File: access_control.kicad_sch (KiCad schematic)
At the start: 64 parts, among them J1 Conn_01x04_Pin, J10 Screw_Terminal_01x02, J2 Screw_Terminal_01x04, J3 Screw_Terminal_01x04, J4 Screw_Terminal_01x02, J5 Screw_Terminal_01x04, J6 Screw_Terminal_01x04, J7 Screw_Terminal_01x02, J8 Screw_Terminal_01x02, J9 Screw_Terminal_01x02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

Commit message: ERC check verified
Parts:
- U3, U4: Manufacturer Part Number MAX3232ESE+ -> (none)
- U5: footprint Package_TO_SOT_THT:TO-220-3_Vertical -> (none)
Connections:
- net C1+ renamed U3_C1+
- net U3_C1+: no longer C20.1, U4.1 (C1+)
- net C1- renamed U3_C1-
- net U3_C1-: no longer C20.2, U4.3 (C1-)
- net C2+ renamed U3_C2+
- net U3_C2+: no longer C21.1, U4.4 (C2+)
- net C2- renamed U3_C2-
- net U3_C2-: no longer C21.2, U4.5 (C2-)
- net V+ renamed U3_V+
- net U3_V+: no longer C23.1, U4.2 (V+)
- net V- renamed U3_V-
- net U3_V-: no longer C24.1, U4.6 (V-)
- new net U4_C1+: C20.1, U4.1 (C1+)
- new net U4_C1-: C20.2, U4.3 (C1-)
- new net U4_C2+: C21.1, U4.4 (C2+)
- new net U4_C2-: C21.2, U4.5 (C2-)
- new net U4_V+: C23.1, U4.2 (V+)
- new net U4_V-: C24.1, U4.6 (V-)
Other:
- moved on the sheet: C1, C2, C20, C21, C22, C23, C24, C3, C4, C5, D1, D2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

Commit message: Assigned footprint and information about the diodes D1-4. Added functional block frames.
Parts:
- D1, D2, D3, D4: footprint (none) -> Diode_SMD:D_SMA-SMB_Universal_Handsoldering; Distributor Link 1 (none) -> http://store.comet.bg/Catalogue/Product/49259/; Distributor Link 2 (none) -> https://www.mouser.bg/ProductDetail/Diotec-Semiconductor/M7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; Distributor Link 3 (none) -> https://www.digikey.bg/en/products/detail/diotec-semiconduc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; LCSC (none) -> C2972759; MPN (none) -> M7; Manufacturer (none) -> Tong Ke / Diotec Semiconductor
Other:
- note added: "Door Control"
- note added: "MCU"
- note added: "Power"
- note added: "RS232/UART"
- note added: "RTC"
- moved on the sheet: BT1, C1, C10, C11, C12, C13, C14, C15, C16, C17, C18, C19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

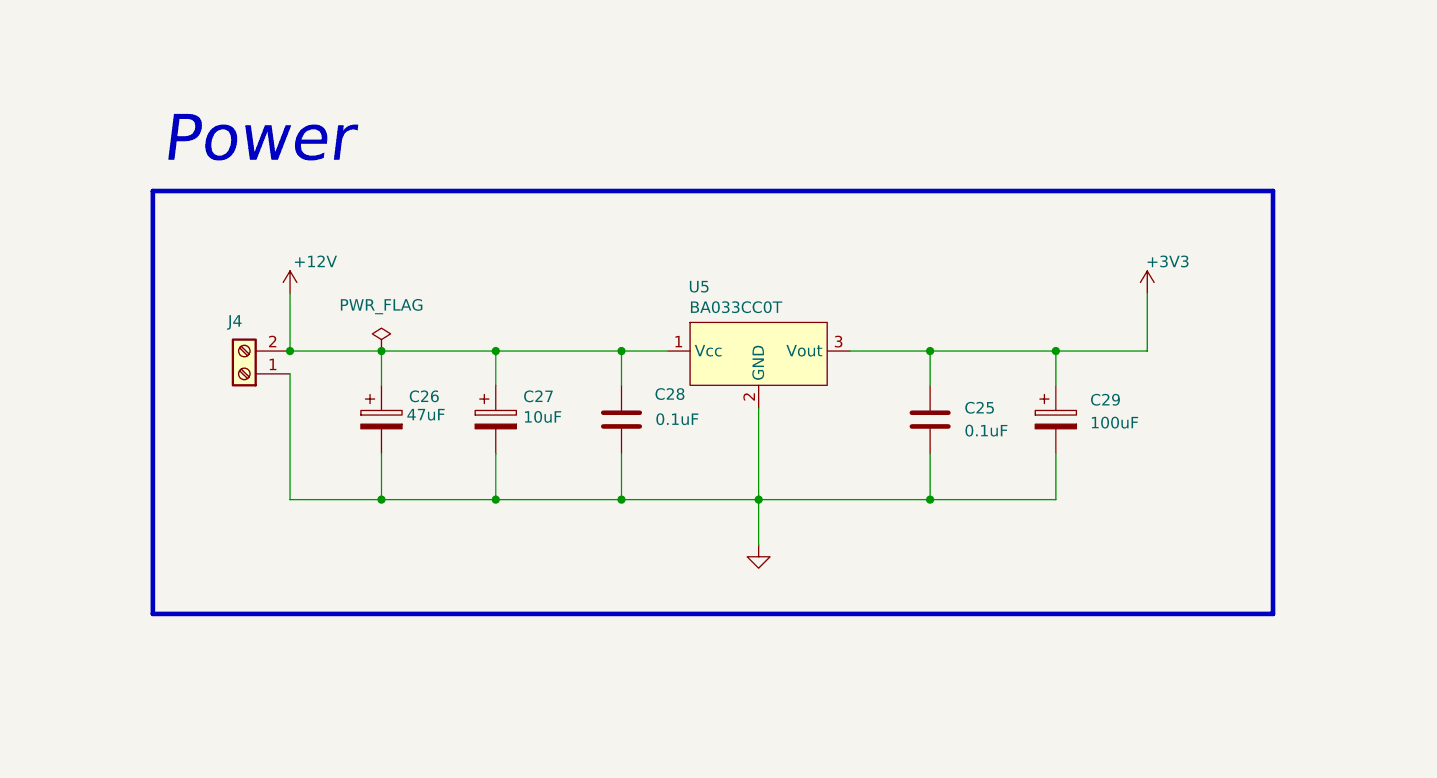
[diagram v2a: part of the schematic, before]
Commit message: Added LED indication for 3.3V
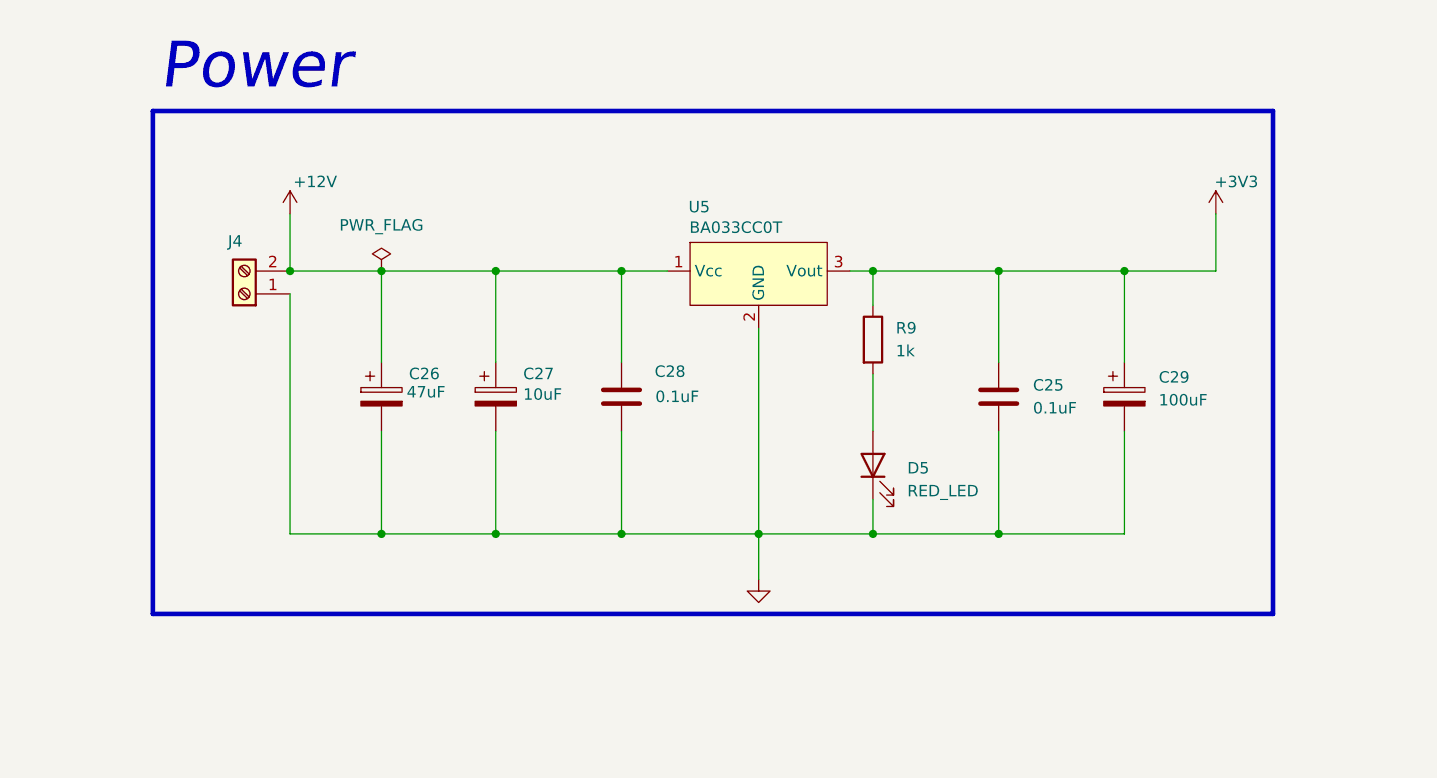
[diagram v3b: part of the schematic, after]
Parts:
- added D5: RED_LED, LED_THT:LED_D3.0mm, symbol Device:LED
- added R9: 1k, Resistor_SMD:R_0805_2012Metric_Pad1.20x1.40mm_HandSolder, symbol Device:R
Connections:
- net +3V3: now also R9.1
- net GND: now also D5.1 (K)
- new net: D5.2 (A), R9.2
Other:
- moved on the sheet: C25, C26, C27, C28, C29, J4, U5

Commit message: Changed the oscillator with another one that is in stock
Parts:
- C14, C15: Distributor Link 3 (none) -> https://store.comet.bg/en/Catalogue/Product/6645/
- C17, C18: Distributor Link 3 (none) -> https://store.comet.bg/en/Catalogue/Product/23048/
- Y1: Distributor Link 1 https://www.digikey.bg/en/products/detail/abracon-llc/ABM8N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 -> https://store.comet.bg/Catalogue/Product/46207/; Distributor Link 2 https://www.mouser.bg/ProductDetail/ABRACON/ABM8N-16.0000MH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 -> (none); LCSC (none) -> C13738; MPN ABM8N-16.0000MHZ-10-B1U-T3 -> X322516MKB4SI; Manufacturer Abracon -> YANGXING TECHNOLOGY Co., Ltd; private KLC_S4.1 -> (none)
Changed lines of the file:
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@@
 			)
 		)
+		(property "Distributor Link 3" "https://store.comet.bg/en/Catalogue/Product/23048/"
+			(at 60.96 204.47 0)
+			(effects
+				(font
+					(size 1.27 1.27)
+				)
+				(hide yes)
+			)
+		)
 		(pin "2"
 		)
@@
 			)
 		)
+		(property "Distributor Link 3" "https://store.comet.bg/en/Catalogue/Product/6645/"
+			(at 148.59 147.32 0)
+			(effects
+				(font
+					(size 1.27 1.27)
+				)
+				(hide yes)
+			)
+		)
 		(pin "1"
 		)
@@
 			)
 		)
-		(property "Description" "CRYSTAL 16.0000MHZ 10PF SMD"
+		(property "Description" "16.000 MHz 3.2x2.5mm SMD (DFN) 10ppm 8pF -20+70°C"
 			(at 67.31 193.04 0)
 			(effects
@@
 			)
 		)
-		(property private "KLC_S3.3" "The rectangle is not a symbol body but a graphical element"
-			(at 67.31 205.74 0)
-			(show_name yes)
+		(property "Manufacturer" "YANGXING TECHNOLOGY Co., Ltd"
+			(at 67.31 193.04 0)
 			(effects
 				(font
@@
 			)
 		)
-		(property private "KLC_S4.1" "Some pins are on 50mil grid to make the symbol small"
-			(at 67.31 208.28 0)
-			(show_name yes)
+		(property "MPN" "X322516MKB4SI"
+			(at 67.31 193.04 0)
 			(effects
 				(font
@@
 			)
 		)
-		(property "Manufacturer" "Abracon"
+		(property "Distributor Link 1" "https://store.comet.bg/Catalogue/Product/46207/"
 			(at 67.31 193.04 0)
 			(effects
@@
 			)
 		)
-		(property "MPN" "ABM8N-16.0000MHZ-10-B1U-T3"
+		(property "LCSC" "C13738"
 			(at 67.31 193.04 0)
 			(effects
@@
 			)
 		)
-		(property "Distributor Link 2" "https://www.mouser.bg/ProductDetail/ABRACON/ABM8N-16.0000MHZ-10-B1U-T3?qs=bN4HulGPsrH47KagwWgHnw%3D%3D"
+		(property "Field9" ""
 			(at 67.31 193.04 0)
 			(effects
@@
 			)
 		)
-		(property "Distributor Link 1" "https://www.digikey.bg/en/products/detail/abracon-llc/ABM8N-16-0000MHZ-10-B1U-T3/26484042?s=N4IgTCBcDaIIICECyAOAcgWgIwDYB0ADEQUgBIBa2BGCWAqhgCoDMIAugL5A"
+		(property "Field10" ""
 			(at 67.31 193.04 0)
 			(effects
@@
 			)
 		)
-		(property "Description" "CAP CER 10pF 50V NP0 0805"
+		(property "Description" "10pF 50V C0G +-0.25pF"
 			(at 74.93 204.47 0)
 			(effects
@@
 			)
 		)
+		(property "Distributor Link 3" "https://store.comet.bg/en/Catalogue/Product/23048/"
+			(at 74.93 204.47 0)
+			(effects
+				(font
+					(size 1.27 1.27)
+				)
+				(hide yes)
+			)
+		)
 		(pin "2"
 		)
@@
 			(at 168.91 147.32 0)
 			(effects
+				(font
+					(size 1.27 1.27)
+				)
+				(hide yes)
+			)
+		)
+		(property "Distributor Link 3" "https://store.comet.bg/en/Catalogue/Product/6645/"
+			(at 168.91 147.32 0)
+			(effects

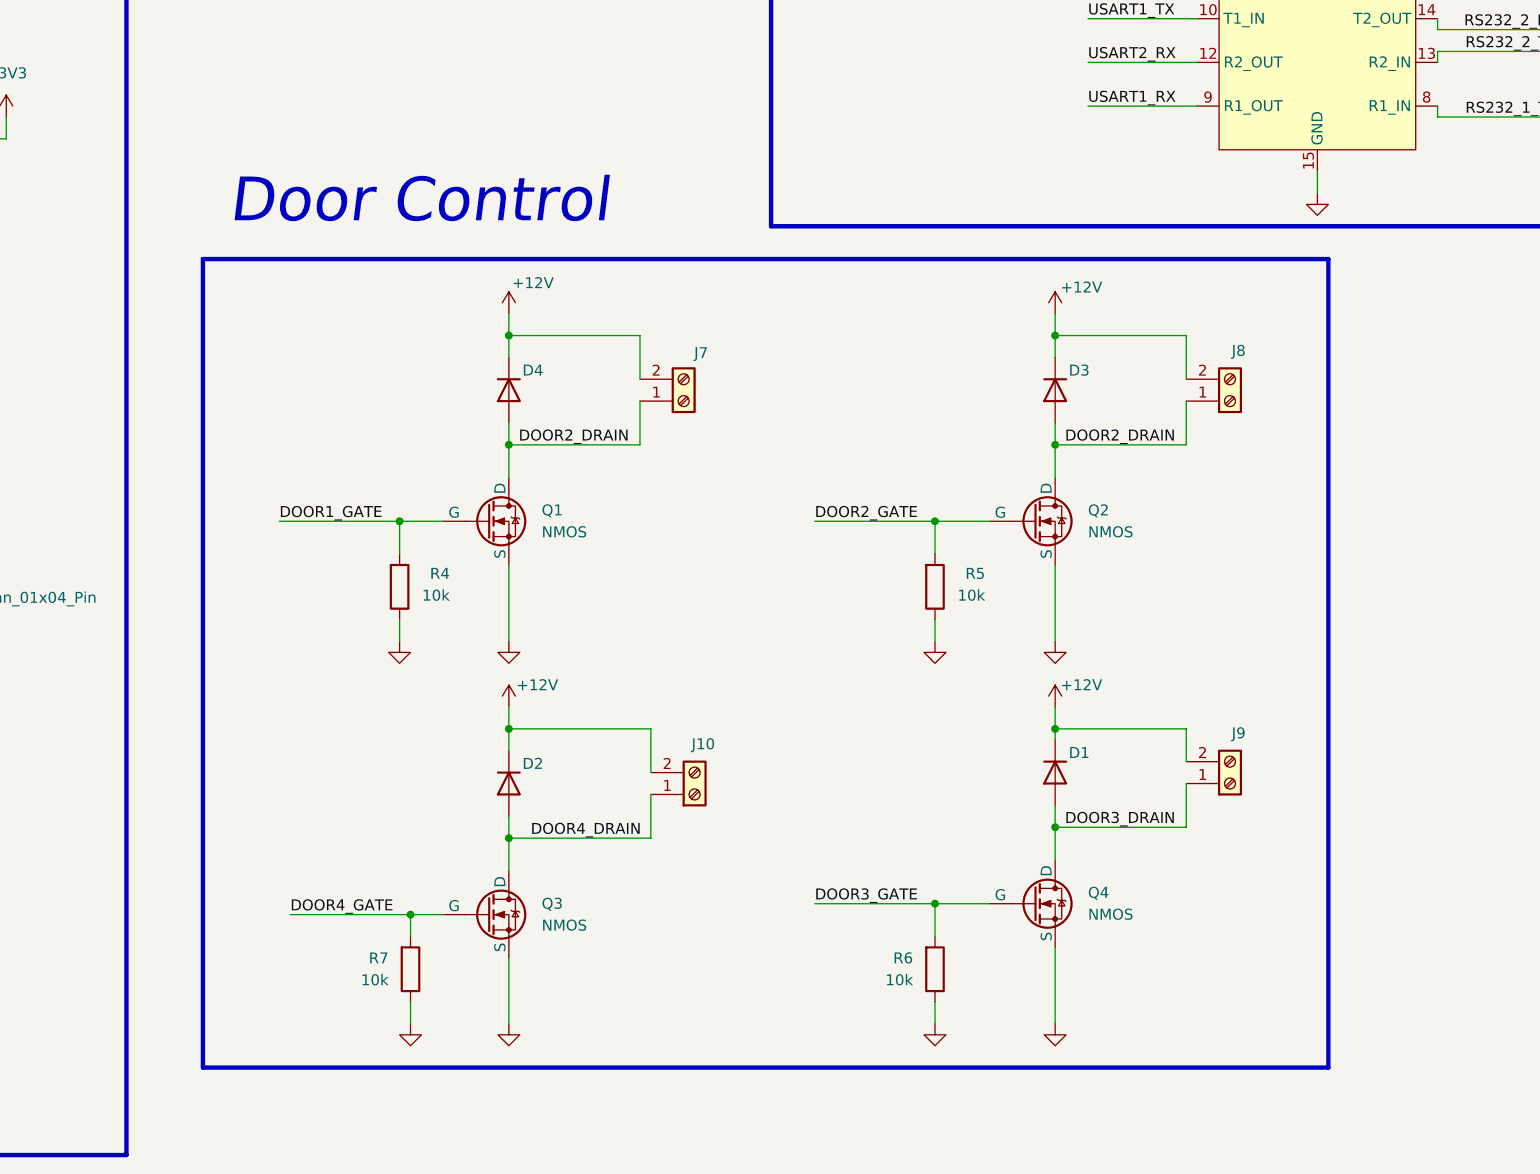
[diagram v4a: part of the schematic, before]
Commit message: Placed 30 Ohms resistors to every transistors gate
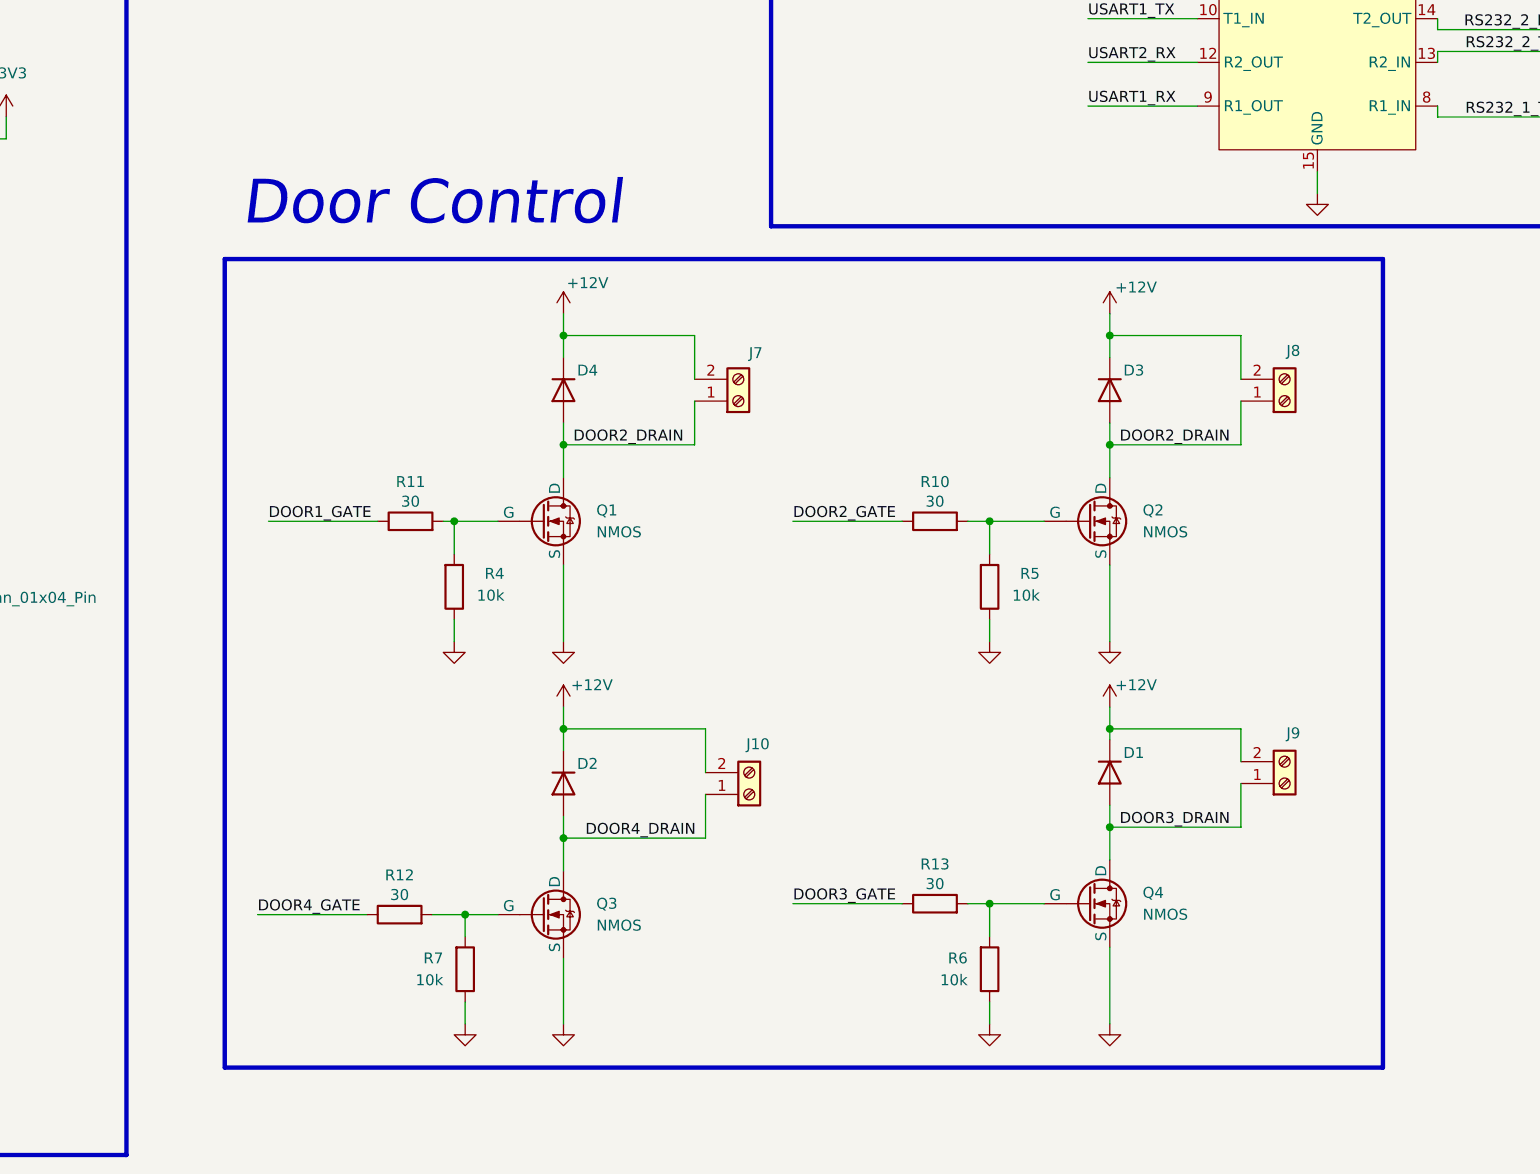
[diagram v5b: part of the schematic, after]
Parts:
- added R10, R11, R12, R13: 30, symbol Device:R
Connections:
- net DOOR1_GATE: now also R11.1; no longer Q1.2 (G), R4.2
- net DOOR2_GATE: now also R10.1; no longer Q2.2 (G), R5.2
- net DOOR3_GATE: now also R13.1; no longer Q4.2 (G), R6.2
- net DOOR4_GATE: now also R12.1; no longer Q3.2 (G), R7.2
- new net: Q1.2 (G), R11.2, R4.2
- new net: Q2.2 (G), R10.2, R5.2
- new net: Q3.2 (G), R12.2, R7.2
- new net: Q4.2 (G), R13.2, R6.2
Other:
- moved on the sheet: D1, D2, D3, D4, J10, J7, J8, J9, Q1, Q2, Q3, Q4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

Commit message: Chnged the VCAP capacitor with another that is in stock
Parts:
- C19: Distributor Link 1 https://www.mouser.bg/ProductDetail/Murata-Electronics/GRM2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 -> (none); Distributor Link 2 https://www.digikey.bg/en/products/detail/murata-electronic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 -> https://www.digikey.bg/en/products/detail/samsung-electro-m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; Distributor Link 3 (none) -> https://store.comet.bg/Catalogue/Product/9581/; LCSC C86040 -> (none); MPN GRM21BR71C475KA73L -> CL21A475KAQNNNE; Manufacturer muRata -> SAMSUNG ELECTRO-MECHANICS
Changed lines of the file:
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@@
 			)
 		)
-		(property "Description" "CAP CER 4.7uF 16V X7R 0805"
+		(property "Description" "4.7uF 25V X5R +-10%"
 			(at 91.44 231.14 0)
 			(effects
@@
 			)
 		)
-		(property "Manufacturer" "muRata"
+		(property "Manufacturer" "SAMSUNG ELECTRO-MECHANICS"
 			(at 91.44 231.14 0)
 			(effects
@@
 			)
 		)
-		(property "MPN" "GRM21BR71C475KA73L"
+		(property "MPN" "CL21A475KAQNNNE"
 			(at 91.44 231.14 0)
 			(effects
@@
 			)
 		)
-		(property "LCSC" "C86040"
+		(property "Distributor Link 2" "https://www.digikey.bg/en/products/detail/samsung-electro-mechanics/CL21A475KAQNNNE/3886902?s=N4IgTCBcDaIMIBkwEYCCAWA7AVgNKoEUA5EgURAF0BfIA"
 			(at 91.44 231.14 0)
 			(effects
@@
 			)
 		)
-		(property "Distributor Link 1" "https://www.mouser.bg/ProductDetail/Murata-Electronics/GRM21BR71C475KA73L?qs=kHCDrmfBqSDNg0vW%2Fm3%2F%252Bw%3D%3D"
+		(property "Distributor Link 3" "https://store.comet.bg/Catalogue/Product/9581/"
 			(at 91.44 231.14 0)
 			(effects
-				(font
-					(size 1.27 1.27)
-				)
-				(hide yes)
-			)
-		)
-		(property "Distributor Link 2" "https://www.digikey.bg/en/products/detail/murata-electronics/GRM21BR71C475KA73L/1033258?s=N4IgTCBcDaIOICUCyYCMAhBB2VBhALFgKwDSAglgMwAyIAugL5A"
-			(at 91.44 231.14 0)
-			(effects

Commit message: Component placement for the PCB is ready.
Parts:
- added D6, D7: D, Diode_SMD:D_SMA-SMB_Universal_Handsoldering, symbol Device:D
- R10, R11, R12, R13: footprint (none) -> Resistor_SMD:R_0805_2012Metric_Pad1.20x1.40mm_HandSolder
- SW1: LCSC (none) -> C22375342; MPN (none) -> TS110416043; Manufacturer (none) -> HanElectricity
- U1: LCSC (none) -> C69336; MPN (none) -> STM32F446RET6; Manufacturer (none) -> ST
- U2: LCSC (none) -> C9866; MPN (none) -> DS3231SN#T&R; Manufacturer (none) -> MAXIM
- U5: footprint (none) -> Package_TO_SOT_THT:TO-220-3_Horizontal_TabDown
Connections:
- net +12V: now also D7.2 (A); no longer C26.1, C27.1, C28.1, U5.1 (Vcc)
- net +3V3: now also D6.2 (A)
- net DOOR2_DRAIN: no longer D4.2 (A), J7.1 (Pin_1), Q1.1 (D)
- new net: C26.1, C27.1, C28.1, D6.1 (K), D7.1 (K), U5.1 (Vcc)
- new net DOOR1_DRAIN: D4.2 (A), J7.1 (Pin_1), Q1.1 (D)
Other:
- moved on the sheet: D5, J4, R9
